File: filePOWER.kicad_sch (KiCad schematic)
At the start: 34 parts, among them U1 FAN53541, U10 NCP115-2.5, U2 FAN53541, U7 FAN53541

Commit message: Update Mouser prices
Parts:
- C1, C12, C46, C47, C77: Pricing (EUR) 0,19 -> 0,17
- C14, C2, C5: Pricing (EUR) 0,11 -> 0,09
- C15, C16, C17, C18, C6, C7: Pricing (EUR) 0,15 -> 0,18
- C3: Pricing (EUR) 0,16 -> 0,18
- D2, D3: Pricing (EUR) 0,38 -> 0,48
- L1, L2, L3: Pricing (EUR) 0,25 -> 0,28
- R15: Pricing (EUR) 0,09 -> 0,11
- R16: Pricing (EUR) 0,09 -> 0,10
- R2: Pricing (EUR) 0,10 -> 0,11
- U1, U2, U7: Pricing (EUR) 1,33 -> 1,82
- U10: Pricing (EUR) 0,29 -> 0,49
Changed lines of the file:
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@@
       (effects (font (size 1.27 1.27)) hide)
     )
-    (property "Pricing (EUR)" "1,33" (id 7) (at 213.36 138.43 0)
+    (property "Pricing (EUR)" "1,82" (id 7) (at 213.36 138.43 0)
       (effects (font (size 1.27 1.27)) hide)
     )
@@
       (effects (font (size 1.27 1.27)) hide)
     )
-    (property "Pricing (EUR)" "0,25" (id 7) (at 234.95 124.46 0)
+    (property "Pricing (EUR)" "0,28" (id 7) (at 234.95 124.46 0)
       (effects (font (size 1.27 1.27)) hide)
     )
@@
       (effects (font (size 1.27 1.27)) hide)
     )
-    (property "Pricing (EUR)" "0,10" (id 7) (at 240.03 148.59 0)
+    (property "Pricing (EUR)" "0,11" (id 7) (at 240.03 148.59 0)
       (effects (font (size 1.27 1.27)) hide)
     )
@@
       (effects (font (size 1.27 1.27)) hide)
     )
-    (property "Pricing (EUR)" "0,15" (id 7) (at 262.89 142.24 0)
+    (property "Pricing (EUR)" "0,18" (id 7) (at 262.89 142.24 0)
       (effects (font (size 1.27 1.27)) hide)
     )
@@
       (effects (font (size 1.27 1.27)) hide)
     )
-    (property "Pricing (EUR)" "0,15" (id 7) (at 267.97 142.24 0)
+    (property "Pricing (EUR)" "0,18" (id 7) (at 267.97 142.24 0)
       (effects (font (size 1.27 1.27)) hide)
     )
@@
       (effects (font (size 1.27 1.27)) hide)
     )
-    (property "Pricing (EUR)" "0,11" (id 7) (at 177.8 129.54 0)
+    (property "Pricing (EUR)" "0,09" (id 7) (at 177.8 129.54 0)
       (effects (font (size 1.27 1.27)) hide)
     )
@@
       (effects (font (size 1.27 1.27)) hide)
     )
-    (property "Pricing (EUR)" "0,19" (id 8) (at 115.57 40.64 0)
+    (property "Pricing (EUR)" "0,17" (id 8) (at 115.57 40.64 0)
       (effects (font (size 1.27 1.27)) hide)
     )
@@
       (effects (font (size 1.27 1.27)) hide)
     )
-    (property "Pricing (EUR)" "1,33" (id 7) (at 213.36 92.71 0)
+    (property "Pricing (EUR)" "1,82" (id 7) (at 213.36 92.71 0)
       (effects (font (size 1.27 1.27)) hide)
     )
@@
       (effects (font (size 1.27 1.27)) hide)
     )
-    (property "Pricing (EUR)" "0,25" (id 7) (at 234.95 78.74 0)
+    (property "Pricing (EUR)" "0,28" (id 7) (at 234.95 78.74 0)
       (effects (font (size 1.27 1.27)) hide)
     )
@@
       (effects (font (size 1.27 1.27)) hide)
     )
-    (property "Pricing (EUR)" "0,09" (id 7) (at 240.03 102.87 0)
+    (property "Pricing (EUR)" "0,10" (id 7) (at 240.03 102.87 0)
       (effects (font (size 1.27 1.27)) hide)
     )
@@
       (effects (font (size 1.27 1.27)) hide)
     )
-    (property "Pricing (EUR)" "0,15" (id 7) (at 262.89 96.52 0)
+    (property "Pricing (EUR)" "0,18" (id 7) (at 262.89 96.52 0)
       (effects (font (size 1.27 1.27)) hide)
     )
@@
       (effects (font (size 1.27 1.27)) hide)
     )
-    (property "Pricing (EUR)" "0,15" (id 7) (at 267.97 96.52 0)
+    (property "Pricing (EUR)" "0,18" (id 7) (at 267.97 96.52 0)
       (effects (font (size 1.27 1.27)) hide)
     )
@@
       (effects (font (size 1.27 1.27)) hide)
     )
-    (property "Pricing (EUR)" "0,11" (id 7) (at 177.8 83.82 0)
+    (property "Pricing (EUR)" "0,09" (id 7) (at 177.8 83.82 0)
       (effects (font (size 1.27 1.27)) hide)
     )
@@
       (effects (font (size 1.27 1.27)) hide)
     )
-    (property "Pricing (EUR)" "1,33" (id 7) (at 213.36 44.45 0)
+    (property "Pricing (EUR)" "1,82" (id 7) (at 213.36 44.45 0)
       (effects (font (size 1.27 1.27)) hide)
     )
@@
       (effects (font (size 1.27 1.27)) hide)
     )
-    (property "Pricing (EUR)" "0,25" (id 7) (at 234.95 30.48 0)
+    (property "Pricing (EUR)" "0,28" (id 7) (at 234.95 30.48 0)
       (effects (font (size 1.27 1.27)) hide)
     )
@@
       (effects (font (size 1.27 1.27)) hide)
     )
-    (property "Pricing (EUR)" "0,09" (id 7) (at 240.03 54.61 0)
+    (property "Pricing (EUR)" "0,11" (id 7) (at 240.03 54.61 0)
       (effects (font (size 1.27 1.27)) hide)
     )
@@
       (effects (font (size 1.27 1.27)) hide)
     )
-    (property "Pricing (EUR)" "0,15" (id 7) (at 262.89 48.26 0)
+    (property "Pricing (EUR)" "0,18" (id 7) (at 262.89 48.26 0)
       (effects (font (size 1.27 1.27)) hide)
     )
@@
       (effects (font (size 1.27 1.27)) hide)
     )
-    (property "Pricing (EUR)" "0,15" (id 7) (at 267.97 48.26 0)
+    (property "Pricing (EUR)" "0,18" (id 7) (at 267.97 48.26 0)
       (effects (font (size 1.27 1.27)) hide)
     )
@@
       (effects (font (size 1.27 1.27)) hide)
     )
-    (property "Pricing (EUR)" "0,16" (id 7) (at 168.91 35.56 0)
+    (property "Pricing (EUR)" "0,18" (id 7) (at 168.91 35.56 0)
       (effects (font (size 1.27 1.27)) hide)
     )
@@
       (effects (font (size 1.27 1.27)) hide)
     )
-    (property "Pricing (EUR)" "0,11" (id 7) (at 175.26 35.56 0)
+    (property "Pricing (EUR)" "0,09" (id 7) (at 175.26 35.56 0)
       (effects (font (size 1.27 1.27)) hide)
     )
@@
       (effects (font (size 1.27 1.27)) hide)
     )
-    (property "Pricing (EUR)" "0,19" (id 8) (at 30.48 39.37 0)
+    (property "Pricing (EUR)" "0,17" (id 8) (at 30.48 39.37 0)
       (effects (font (size 1.27 1.27)) hide)
     )
@@
       (effects (font (size 1.27 1.27)) hide)
     )
-    (property "Pricing (EUR)" "0,29" (id 7) (at 85.09 116.84 0)
+    (property "Pricing (EUR)" "0,49" (id 7) (at 85.09 116.84 0)
       (effects (font (size 1.27 1.27)) hide)
     )
@@
       (effects (font (size 1.27 1.27)) hide)
     )
-    (property "Pricing (EUR)" "0,19" (id 8) (at 55.88 119.38 0)
+    (property "Pricing (EUR)" "0,17" (id 8) (at 55.88 119.38 0)
       (effects (font (size 1.27 1.27)) hide)
     )
@@
       (effects (font (size 1.27 1.27)) hide)
     )
-    (property "Pricing (EUR)" "0,19" (id 8) (at 104.14 119.38 0)
+    (property "Pricing (EUR)" "0,17" (id 8) (at 104.14 119.38 0)
       (effects (font (size 1.27 1.27)) hide)
     )
@@
       (effects (font (size 1.27 1.27)) hide)
     )
-    (property "Pricing (EUR)" "0,38" (id 7) (at 71.12 35.56 0)
+    (property "Pricing (EUR)" "0,48" (id 7) (at 71.12 35.56 0)
       (effects (font (size 1.27 1.27)) hide)
     )
@@
       (effects (font (size 1.27 1.27)) hide)
     )
-    (property "Pricing (EUR)" "0,38" (id 7) (at 71.12 58.42 0)
+    (property "Pricing (EUR)" "0,48" (id 7) (at 71.12 58.42 0)
       (effects (font (size 1.27 1.27)) hide)
     )
@@
       (effects (font (size 1.27 1.27)) hide)
     )
-    (property "Pricing (EUR)" "0,19" (id 8) (at 30.48 62.23 0)
-      (effects (font (size 1.27 1.27)) hide)
-    )
+    (property "Pricing (EUR)" "0,17" (id 8) (at 30.48 62.23 0)
+      (effects (font (size 1.27 1.27)) hide)
+    )

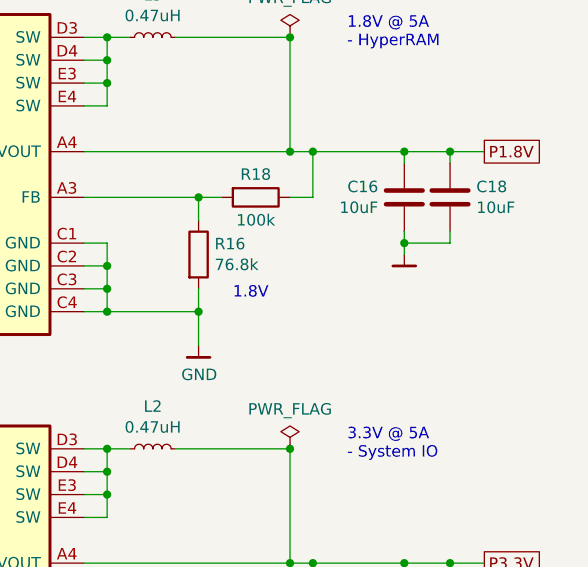
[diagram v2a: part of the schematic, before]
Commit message: Replace HyperRAM with 3V Winbond part
Also remove PSC/PSC# as they are not used on 3V parts.
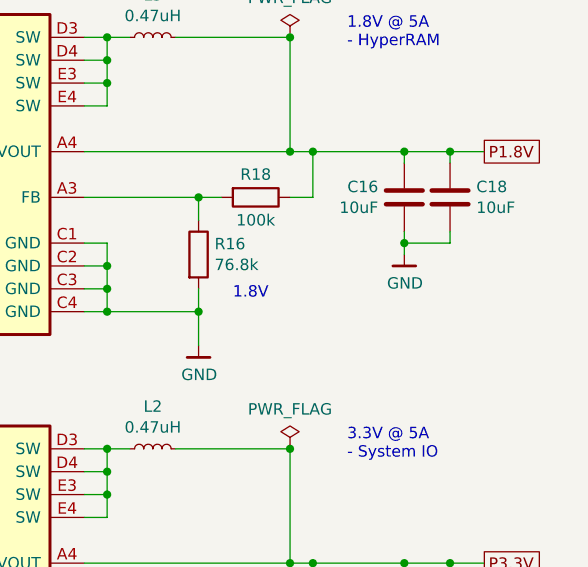
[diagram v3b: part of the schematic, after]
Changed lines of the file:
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@@
       (effects (font (size 1.27 1.27)) hide)
     )
-    (property "Value" "" (id 1) (at 262.9662 106.0704 0))
+    (property "Value" "GND" (id 1) (at 262.9662 106.0704 0))
     (property "Footprint" "" (id 2) (at 260.35 111.76 0)
       (effects (font (size 1.27 1.27)) hide)

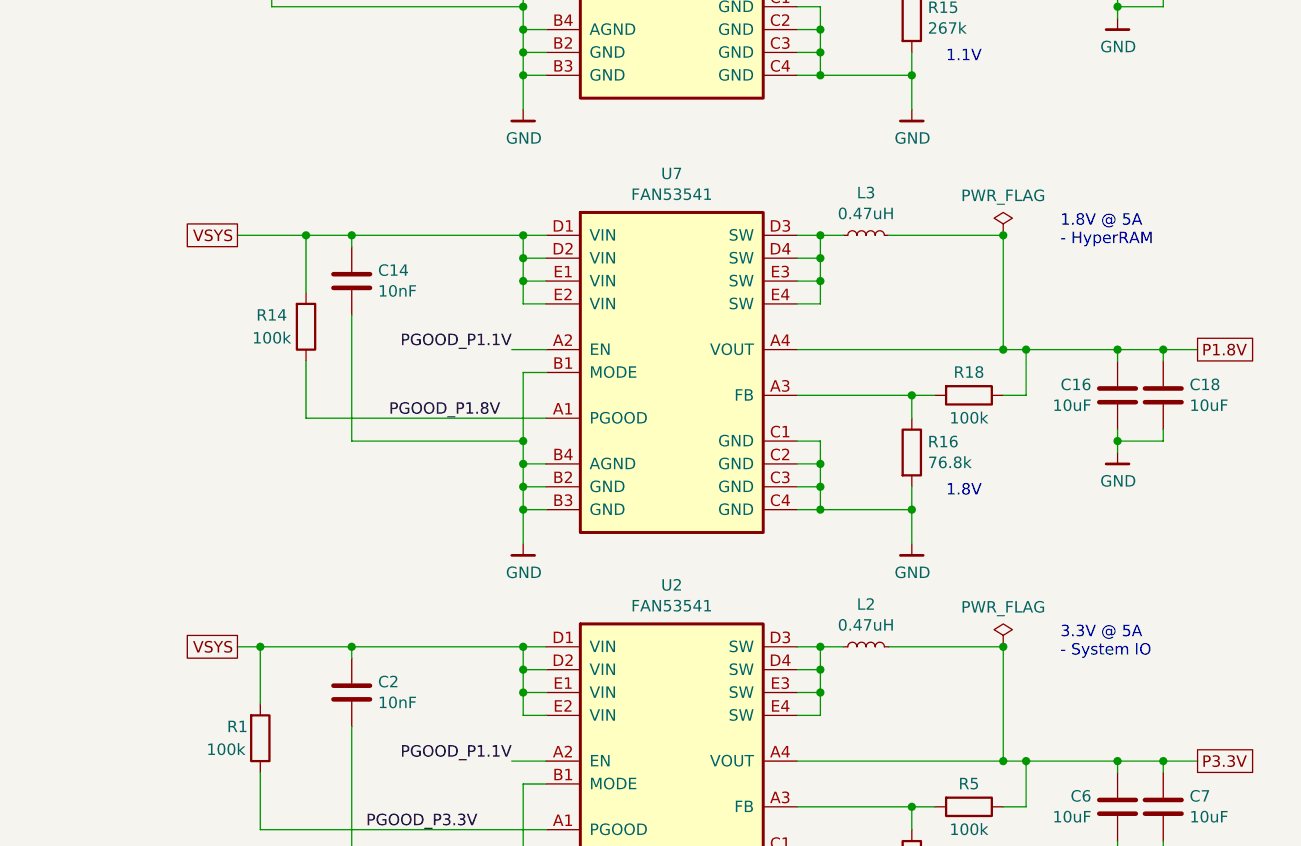
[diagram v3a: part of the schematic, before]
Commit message: Remove 1.8V power supply
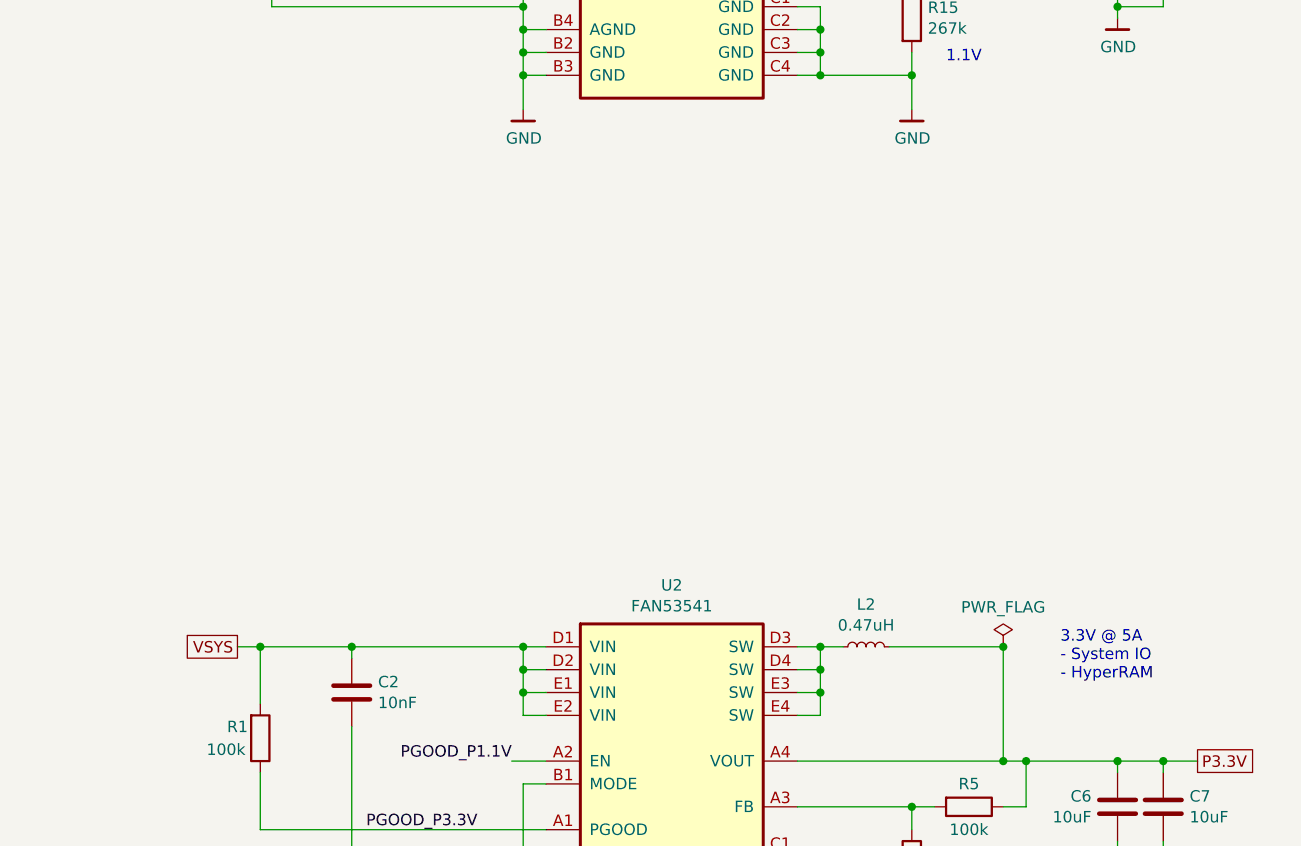
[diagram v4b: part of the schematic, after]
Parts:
- removed C14: 10nF, Capacitor_SMD:C_0201_0603Metric, symbol Device:C
- removed C16, C18: 10uF, Capacitor_SMD:C_0402_1005Metric, symbol Device:C
- removed L3: 0.47uH, Inductor_SMD:L_0805_2012Metric, symbol Device:L_Small
- removed R14, R18: 100k, Resistor_SMD:R_0201_0603Metric, symbol Device:R
- removed R16: 76.8k, Resistor_SMD:R_0201_0603Metric, symbol Device:R
- removed U7: FAN53541, Package_CSP:WLCSP-20_1.934x2.434mm_Layout4x5_P0.4mm, symbol gkl_pmic:FAN53541
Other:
- note added: "3.3V @ 5A - System IO - HyperRAM"
- note removed: "1.8V"
- note removed: "1.8V @ 5A - HyperRAM"
- note removed: "3.3V @ 5A - System IO"

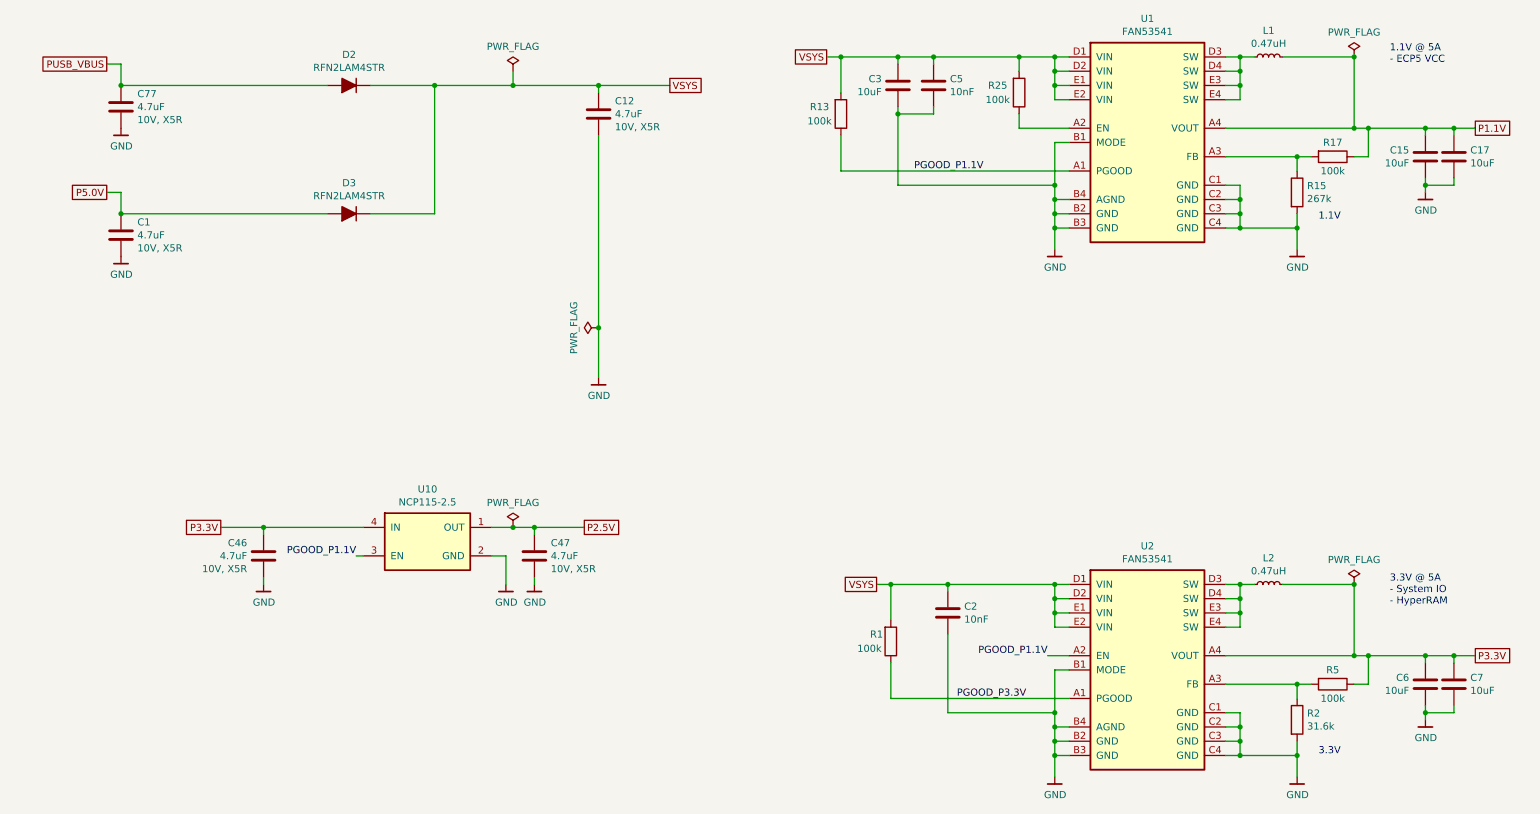
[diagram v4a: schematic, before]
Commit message: Add USB-C power management chip
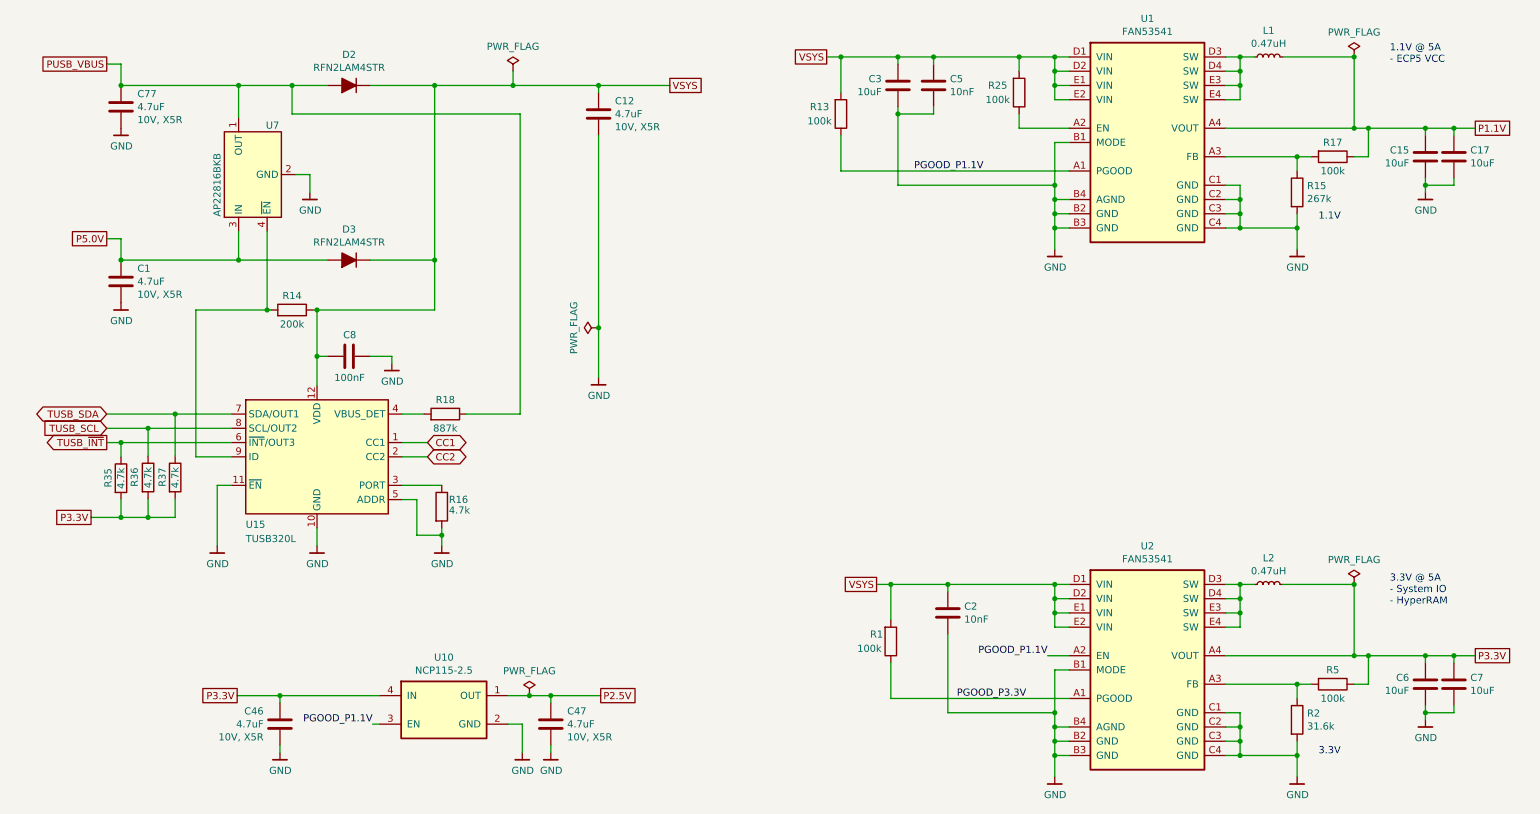
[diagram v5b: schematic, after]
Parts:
- added C8: 100nF, Capacitor_SMD:C_0201_0603Metric, symbol Device:C
- added R14: 200k, Resistor_SMD:R_0201_0603Metric, symbol Device:R
- added R16, R35, R36, R37: 4.7k, Resistor_SMD:R_0402_1005Metric, symbol Device:R
- added R18: 887k, Resistor_SMD:R_0201_0603Metric, symbol Device:R
- added U15: TUSB320L, Package_DFN_QFN:Texas_X2QFN-12_1.6x1.6mm_P0.4mm, symbol Interface_USB:TUSB320
- added U7: AP22816BKB, Package_TO_SOT_SMD:SOT-23-5, symbol Power_Management:AP22804BW5
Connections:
- net GND: now also C8.2, R16.2, U15.10 (GND), U15.11 (~{EN}), U15.5 (ADDR), U7.2 (GND)
- net P3.3V: now also R35.2, R36.2, R37.2
- net P5.0V: now also U7.3 (IN)
- net PUSB_VBUS: now also R18.1, U7.1 (OUT), U7.5 (OUT)
- net VSYS: now also C8.1, R14.1, U15.12 (VDD)
- new net: R16.1, U15.3 (PORT)
- new net: R18.2, U15.4 (VBUS_DET)
- new net: R14.2, U15.9 (ID), U7.4 (~{EN})
- new net CC1: U15.1 (CC1)
- new net CC2: U15.2 (CC2)
- new net TUSB_SCL: R36.1, U15.8 (SCL/OUT2)
- new net TUSB_SDA: R37.1, U15.7 (SDA/OUT1)
- new net TUSB_~{INT}: R35.1, U15.6 (~{INT}/OUT3)
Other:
- moved on the sheet: C1, C46, C47, D3, U10
